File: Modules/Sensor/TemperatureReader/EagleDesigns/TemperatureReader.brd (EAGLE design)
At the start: 100 x 80 mm, 11 parts, among them U1 MLX90614, U2 ATMEGA328P_TQFP

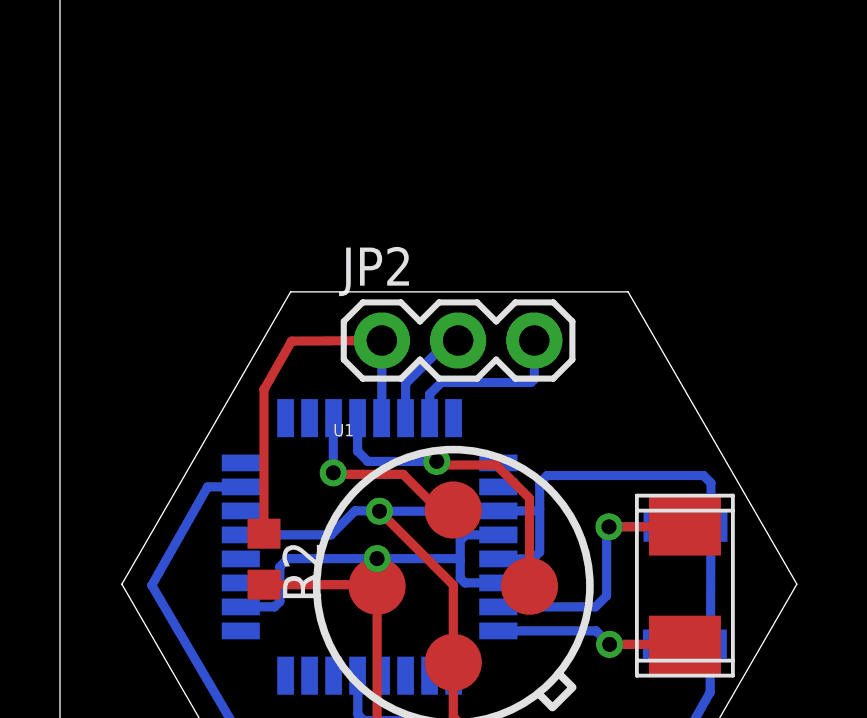
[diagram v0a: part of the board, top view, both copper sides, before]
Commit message: finalized TemperatureReader layout for #31
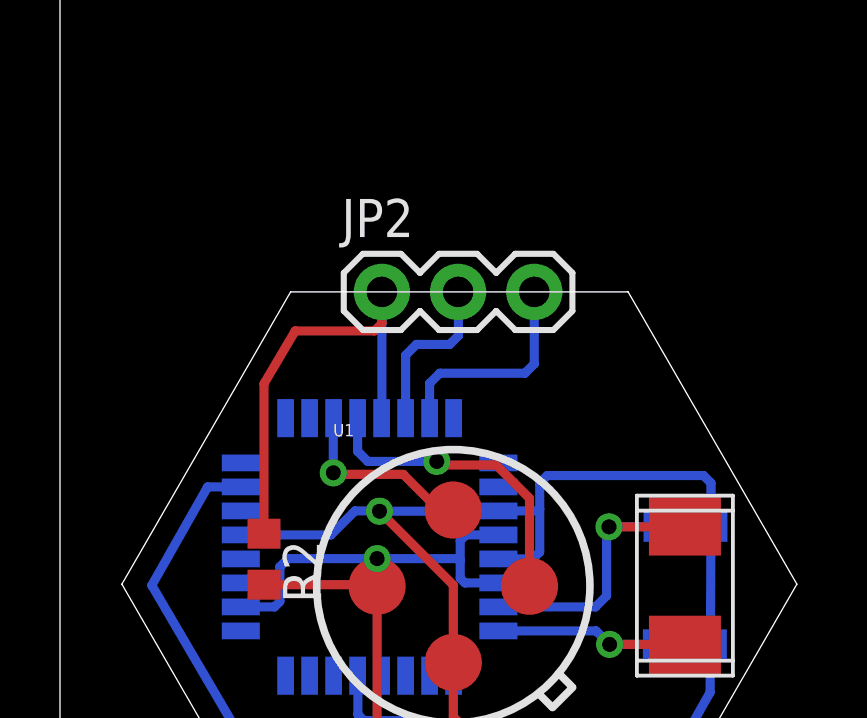
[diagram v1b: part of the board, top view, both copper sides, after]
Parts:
- moved JP2 1.62 mm to (10.7, 21.8)
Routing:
- net RESET: track 12.3 -> 15.3 mm
- net RX: track 3.49 -> 5.59 mm
- net TX: track 5.78 -> 7.32 mm
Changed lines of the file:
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@@
 <setting verticaltext="up"/>
 </settings>
-<grid distance="0.01" unitdist="mm" unit="mm" style="lines" multiple="1" display="no" altdistance="0.025" altunitdist="inch" altunit="inch"/>
+<grid distance="0.01" unitdist="mm" unit="mm" style="lines" multiple="1" display="yes" altdistance="0.025" altunitdist="inch" altunit="inch"/>
 <layers>
 <layer number="1" name="Top" color="4" fill="1" visible="yes" active="yes"/>
@@
 <element name="JP1" library="SparkFun-Connectors" package="1X04" value="" x="17.17" y="3.9" rot="R180"/>
 <element name="R1" library="adafruit" package="R0603" value="1M" x="7.79" y="6.53" rot="MR0"/>
-<element name="JP2" library="SparkFun-Connectors" package="1X03" value="" x="10.73" y="20.16"/>
+<element name="JP2" library="SparkFun-Connectors" package="1X03" value="" x="10.73" y="21.78"/>
 <element name="U2" library="SparkFun-DigitalIC" package="TQFP32-08" value="ATMEGA328P_TQFP" x="10.32" y="13.28" rot="MR0">
 <attribute name="PROD_ID" value="IC-09069" x="20.38" y="10.84" size="1.778" layer="28" rot="MR0" display="off"/>
@@
 <contactref element="U2" pad="29"/>
 <contactref element="R2" pad="1"/>
-<wire x1="10.73" y1="20.16" x2="10.73" y2="17.5826" width="0.3048" layer="16"/>
+<wire x1="10.73" y1="21.78" x2="10.73" y2="17.5826" width="0.3048" layer="16"/>
 <wire x1="10.73" y1="17.5826" x2="10.72" y2="17.5726" width="0.3048" layer="16"/>
-<wire x1="6.8" y1="13.72" x2="6.8" y2="18.54" width="0.3048" layer="1"/>
-<wire x1="6.8" y1="18.54" x2="6.82" y2="18.56" width="0.3048" layer="1"/>
-<wire x1="6.82" y1="18.56" x2="7.72" y2="20.14" width="0.3048" layer="1"/>
-<wire x1="7.72" y1="20.14" x2="10.73" y2="20.16" width="0.3048" layer="1"/>
+<wire x1="6.8" y1="13.72" x2="6.8" y2="18.72" width="0.3048" layer="1"/>
+<wire x1="6.8" y1="18.72" x2="7.84" y2="20.48" width="0.3048" layer="1"/>
+<wire x1="7.84" y1="20.48" x2="10.48" y2="20.48" width="0.3048" layer="1"/>
+<wire x1="10.48" y1="20.48" x2="10.73" y2="20.73" width="0.3048" layer="1"/>
+<wire x1="10.73" y1="20.73" x2="10.73" y2="21.78" width="0.3048" layer="1"/>
 </signal>
 <signal name="RX">
 <contactref element="JP2" pad="2"/>
 <contactref element="U2" pad="30"/>
-<wire x1="13.27" y1="20.16" x2="12.97" y2="20.16" width="0.3048" layer="16"/>
-<wire x1="12.97" y1="20.16" x2="12.75" y2="19.95" width="0.3048" layer="16"/>
-<wire x1="12.75" y1="19.95" x2="11.52" y2="18.72" width="0.3048" layer="16"/>
-<wire x1="11.52" y1="18.72" x2="11.52" y2="17.5726" width="0.3048" layer="16"/>
+<wire x1="11.52" y1="17.5726" x2="11.52" y2="19.67" width="0.3048" layer="16"/>
+<wire x1="11.52" y1="19.67" x2="11.88" y2="20.03" width="0.3048" layer="16"/>
+<wire x1="11.88" y1="20.03" x2="12.99" y2="20.03" width="0.3048" layer="16"/>
+<wire x1="12.99" y1="20.03" x2="13.28" y2="20.32" width="0.3048" layer="16"/>
+<wire x1="13.28" y1="20.32" x2="13.28" y2="21.77" width="0.3048" layer="16"/>
+<wire x1="13.28" y1="21.77" x2="13.27" y2="21.78" width="0.3048" layer="16"/>
 </signal>
 <signal name="TX">
 <contactref element="JP2" pad="3"/>
 <contactref element="U2" pad="31"/>
-<wire x1="12.32" y1="17.5726" x2="12.32" y2="18.37" width="0.3048" layer="16"/>
-<wire x1="12.32" y1="18.37" x2="12.71" y2="18.76" width="0.3048" layer="16"/>
-<wire x1="12.71" y1="18.76" x2="15.7" y2="18.76" width="0.3048" layer="16"/>
-<wire x1="15.7" y1="18.76" x2="15.81" y2="18.87" width="0.3048" layer="16"/>
-<wire x1="15.81" y1="18.87" x2="15.81" y2="20.16" width="0.3048" layer="16"/>
+<wire x1="15.81" y1="21.78" x2="15.81" y2="19.38" width="0.3048" layer="16"/>
+<wire x1="15.81" y1="19.38" x2="15.5" y2="19.07" width="0.3048" layer="16"/>
+<wire x1="15.5" y1="19.07" x2="12.66" y2="19.07" width="0.3048" layer="16"/>
+<wire x1="12.66" y1="19.07" x2="12.32" y2="18.73" width="0.3048" layer="16"/>
+<wire x1="12.32" y1="18.73" x2="12.32" y2="17.5726" width="0.3048" layer="16"/>
 </signal>
 <signal name="1X3SIN">
